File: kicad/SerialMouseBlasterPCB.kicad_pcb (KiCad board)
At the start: 2 copper layers, 51.1 x 24.3 mm, 34 parts, among them J1 Conn_01x05, J2 Conn_01x04_Male, J3 Conn_01x03_Male, U1 ICM7555xP, U2 LM358, U3 RaspberryPi_Pico

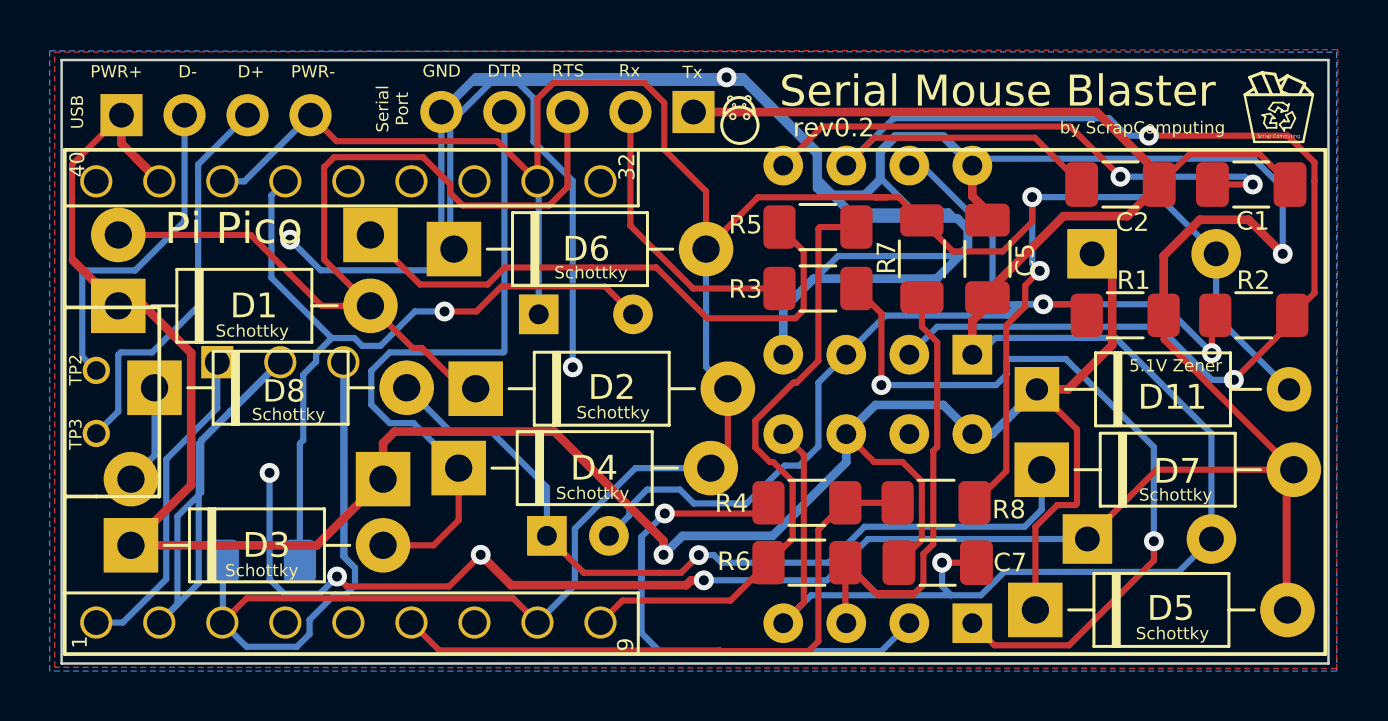
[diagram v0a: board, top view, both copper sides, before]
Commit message: Rev 0.3: All components are SMD and the board is much smaller
- Footprint is much smaller and the gap between the Pico and the PCB can be minimal
- All SMD components are on one side of the board, which makes them accessible even when the Pico is soldered on
- Capacitor values have been reduced
- Pico reset is now fixed with the use of a PNP bleeder transistor
- All component values are now printed on the PCB
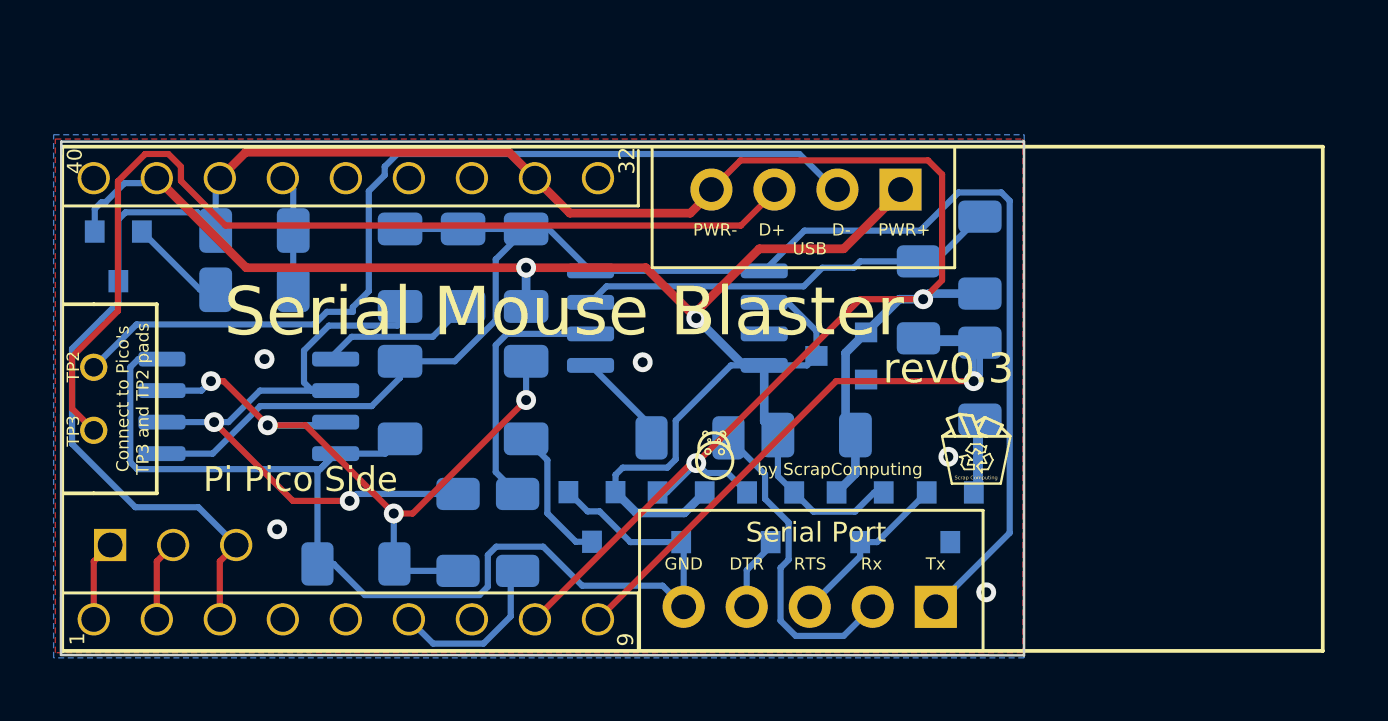
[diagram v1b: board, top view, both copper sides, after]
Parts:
- removed C5: 1uF, Capacitor_SMD:C_1206_3216Metric_Pad1.33x1.80mm_HandSolder
- removed D10, D6, D7, D8: 1N5817, Diode_THT:D_DO-41_SOD81_P10.16mm_Horizontal
- removed D9: 1N4001, Diode_THT:D_DO-41_SOD81_P10.16mm_Horizontal
- removed R9: 1M, Resistor_SMD:R_1206_3216Metric_Pad1.30x1.75mm_HandSolder
- added Q1: MMBTA92, Package_TO_SOT_SMD:SOT-23, B.Cu at (127.3, 62.5)
- C1, C2, C7, R1, R2, R3, R4, R5, R6, R7: moved to B.Cu
- C3: footprint Capacitor_THT:CP_Radial_D6.3mm_P2.50mm -> Capacitor_SMD:C_1206_3216Metric_Pad1.33x1.80mm_HandSolder
- C4, C6: value 470uF -> 10uF; footprint Capacitor_THT:CP_Radial_D10.0mm_P5.00mm -> Capacitor_SMD:C_1206_3216Metric_Pad1.33x1.80mm_HandSolder
- C8: value 100uF -> 10uF; footprint Capacitor_THT:CP_Radial_D8.0mm_P3.80mm -> Capacitor_SMD:C_1206_3216Metric_Pad1.33x1.80mm_HandSolder
- D1, D2, D3, D4, D5: value 1N5817 -> BAS40-04; footprint Diode_THT:D_DO-41_SOD81_P10.16mm_Horizontal -> Package_TO_SOT_SMD:SOT-23; moved to B.Cu
- D11: value 1N5231 -> BZX84-C5V1; footprint Diode_THT:D_A-405_P10.16mm_Horizontal -> Diode_SMD:D_SOT-23_ANK; moved to B.Cu
- R8: value 1M -> 1K; footprint Resistor_SMD:R_1206_3216Metric_Pad1.30x1.75mm_HandSolder -> Capacitor_SMD:C_1206_3216Metric_Pad1.33x1.80mm_HandSolder; moved to B.Cu
- U1, U2: footprint Package_DIP:DIP-8_W7.62mm_Socket -> Package_SO:SO-8_5.3x6.2mm_P1.27mm
- moved R2 33.2 mm to (141.0, 73.7), turned to 270 degrees
- moved R1 32.6 mm to (136.9, 74.9), turned to 0 degrees
- moved C1 31.9 mm to (141.2, 63.0), turned to 90 degrees
- moved J2 31.5 mm to (158.9, 59.8), turned to 90 degrees
- moved D1 31.1 mm to (157.2, 73.1), turned to 270 degrees
- moved U1 29.2 mm to (132.6, 68.6), turned to 0 degrees
- moved C2 29.2 mm to (138.7, 63.0), turned to 90 degrees
- moved R8 28.8 mm to (132.8, 63.9)
- moved C6 28.3 mm to (138.7, 68.3), turned to 90 degrees
- moved D3 22.2 mm to (150.0, 73.1), turned to 270 degrees
- moved J1 22.2 mm to (160.3, 76.7)
- moved C7 20.4 mm to (143.8, 63.0), turned to 90 degrees
- moved U2 17.1 mm to (149.9, 65.0), turned to 0 degrees
- moved C4 13.3 mm to (155.5, 69.7)
- moved D2 13.0 mm to (153.6, 73.1), turned to 270 degrees
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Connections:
- C8 pad 1: /PWR- -> Net-(C8-Pad1)
- C8 pad 2: Net-(C8-Pad2) -> /PWR-
- D1 pad 1: /PWR+ -> /PWR-
- D1 pad 2: /RTS -> /PWR+
- D2 pad 1: /RTS -> /PWR-
- D2 pad 2: /PWR- -> /PWR+
- D3 pad 1: /PWR+ -> /PWR-
- D3 pad 2: /DTR -> /PWR+
- D4 pad 1: /DTR -> /GND
- D4 pad 2: /PWR- -> /PWR+
- D5 pad 1: /PWR+ -> /RTS
- D5 pad 2: /GND -> Net-(D5-Pad2)
- R5 pad 1: Net-(D9-Pad1) -> Net-(D5-Pad2)
- R8 pad 1: /PWR- -> Net-(C8-Pad1)
- R8 pad 2: /RxIN -> Net-(Q1-Pad2)
- U3 pad 37: Net-(C8-Pad2) -> Net-(C8-Pad1)
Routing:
- net /GND: track 230.1 -> 47.6 mm, vias 8 -> 5
- net /PWR-: track 142.9 -> 103.0 mm
- net Net-(C8-Pad2): track 30.9 -> 0.00 mm, vias 1 -> 0
- net /RTS: track 37.8 -> 6.96 mm
- net Net-(C2-Pad1): track 55.8 -> 26.7 mm
- net /PWR+: track 101.5 -> 73.0 mm, vias 1 -> 2
- net Net-(R3-Pad1): track 31.2 -> 3.94 mm, vias 2 -> 0
- net Net-(C3-Pad1): track 32.7 -> 5.63 mm, vias 1 -> 0
- net /PicoRx: track 27.9 -> 3.27 mm
- net /D+: track 16.1 -> 40.2 mm
- net /DTR: track 26.8 -> 3.01 mm
- net /D-: track 13.4 -> 36.8 mm
- net Net-(D9-Pad1): track 23.3 -> 0.00 mm
- net /TX: track 84.6 -> 64.6 mm, vias 1 -> 0
- net /RxIN: track 25.2 -> 6.91 mm
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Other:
- board size 51.1 x 24.3 mm -> 38.8 x 20.7 mm
- board text added: "555"
- board text added: "BAS40-04"
- board text added: "CMOS"
- board text added: "Connect to Pico's TP3 and TP2 pads"
- board text added: "LM358"
- board text added: "PNP"
- board text added: "Pi Pico Side"
- board text added: "Zener"
- board text added: "rev0.3"
- board text removed: "+"
- board text removed: "5.1V Zener"
- board text removed: "7555 CMOS Timer"
- board text removed: "LM358N"
- board text removed: "Negative Rail Smoothing Cap"
- board text removed: "Pi Pico"
- board text removed: "Pico Reset Cap"
- board text removed: "Positive Rail Smoothing Cap"
- board text removed: "Schottky"
- board text removed: "Voltage Doubler Cap"
- board text removed: "rev0.2"

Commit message: Rev 0.4: Support positive Tx and add protection diode for 555.
This also changes some resistor and capacitor values to make it easier to assemble.
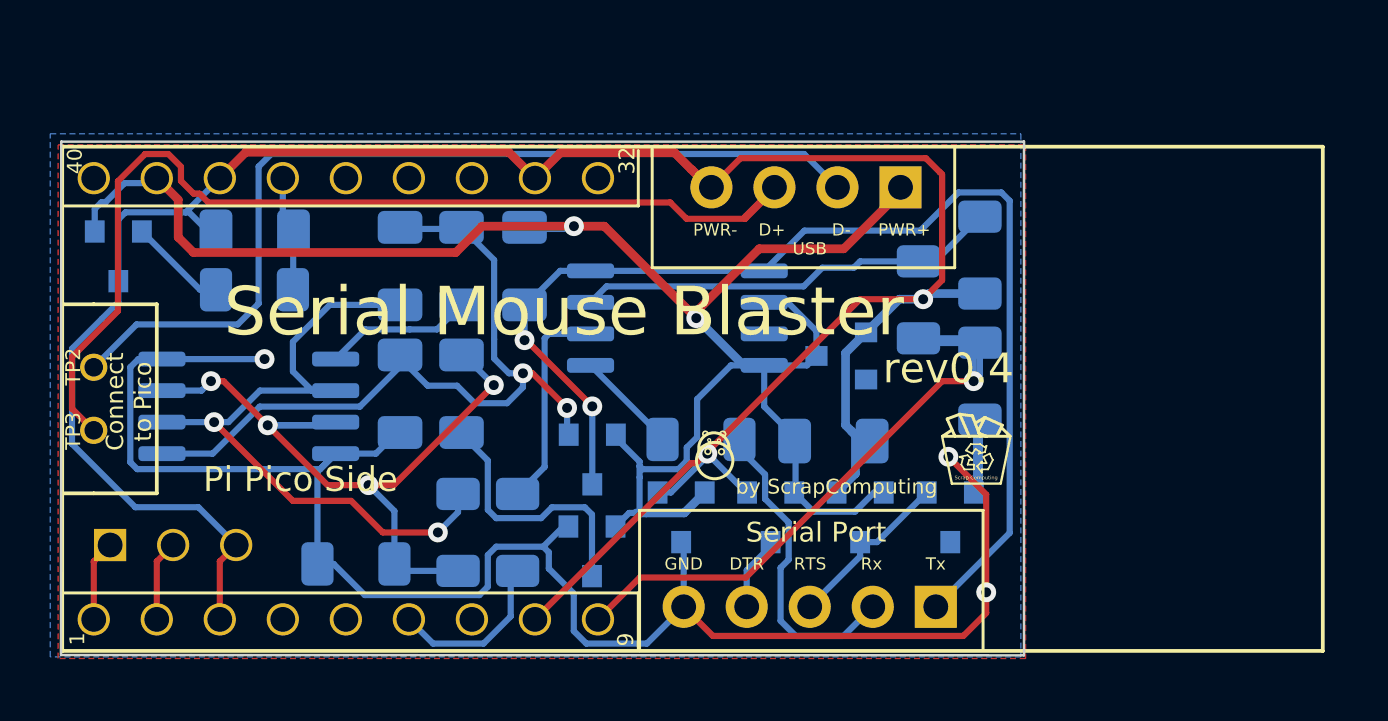
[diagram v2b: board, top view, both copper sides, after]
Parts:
- added D6: BAS40-04, Package_TO_SOT_SMD:SOT-23, B.Cu at (146.4, 70.7)
- C1: value 100nF -> 1uF
- R1: value 4.7K -> 1K
- R2: value 47K -> 22K
- R4: value 100K -> 1K
- R8: footprint Capacitor_SMD:C_1206_3216Metric_Pad1.33x1.80mm_HandSolder -> Resistor_SMD:R_1206_3216Metric_Pad1.30x1.75mm_HandSolder
- moved C3 2.62 mm to (141.2, 68.1)
- moved D4 1.38 mm to (146.4, 74.4)
- moved C4 0.72 mm to (156.1, 70.0)
- moved R3 0.45 mm to (150.8, 69.9)
- moved C6 0.25 mm to (138.7, 68.1)
- moved C7 0.09 mm to (143.7, 62.9), turned to 270 degrees
- moved C1 0.09 mm to (141.2, 62.9)
- moved J2 0.09 mm to (158.9, 59.8)
- moved C2 0.06 mm to (138.7, 62.9)
- moved C8 0.05 mm to (132.8, 61.5)
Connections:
- C1 pad 2: /TX -> Net-(C1-Pad2)
- C2 pad 2: /TX -> Net-(C1-Pad2)
- C6 pad 2: /TX -> Net-(C1-Pad2)
- U1 pad 1: /TX -> Net-(C1-Pad2)
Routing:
- net Net-(C1-Pad2): track 0.00 -> 31.8 mm, vias 0 -> 2
- net /GND: track 47.6 -> 69.8 mm, vias 5 -> 3
- net /TX: track 64.6 -> 47.8 mm, vias 0 -> 2
- net Net-(C3-Pad1): track 5.63 -> 10.9 mm
- net /PWR+: track 73.0 -> 78.0 mm
- net Net-(C2-Pad1): track 26.7 -> 28.6 mm
- net Net-(R4-Pad2): track 10.4 -> 8.65 mm
- net /D+: track 40.2 -> 41.7 mm
- net /PWR-: track 103.0 -> 104.3 mm
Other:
- board text added: "+"
- board text added: "10uF"
- board text added: "Connect to Pico"
- board text added: "TP2"
- board text added: "TP3"
- board text added: "rev0.4"
- board text removed: "Connect to Pico's TP3 and TP2 pads"
- board text removed: "rev0.3"
